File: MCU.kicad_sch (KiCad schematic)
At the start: 0 parts

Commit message: Connected the nucleo to local nets
 - I created all the local lables to the MCU schematic and connected them to the corresponding pins of the Nucleo board.
 - I renumed the hierarchical sheets to be in order of importance
 - I added solder jumpers for making the board more versatile in some cases
 - Corrected the Nucleo pinout on the schematic symbol
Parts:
- added JP? (x6): 0R, symbol Jumper:Jumper_2_Small_Bridged
- added SW?: RESET, Button_Switch_SMD:SW_SPST_SKQG_WithoutStem, symbol Switch:SW_Push
- added U?: NUCLEO64-H503RB, ProjectConnectors:Nucleo64, symbol ProjectMCUs:NUCLEO64-H503RB
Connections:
- new net BTN1: U?.35 (PC2)
- new net BTN2: U?.59 (PC7)
- new net BTN3: U?.1 (PC10)
- new net BTN4: U?.3 (PC12)
- new net BTN5: U?.23 (PC13/BTN2)
- new net BUZZER: JP?.2 (B), JP?.2 (B)
- new net BUZZER_TIM2: U?.28 (PA0)
- new net BUZZER_TIM3: JP?.1 (A), U?.65 (PB4)
- new net E5V: U?.6 (E5V)
- new net GND: SW?.2, U?.19 (GND), U?.20 (GND), U?.22 (GND), U?.47 (GND), U?.58 (GND), U?.8 (GND)
- new net GNDA: U?.70 (AGND)
- new net I2C1_SCL: JP?.1 (A), JP?.2 (B), U?.71 (PC8)
- new net I2C1_SDA: JP?.1 (A), U?.63 (PB10)
- new net I2C_SDA: JP?.2 (B)
- new net I_SENSE: U?.30 (PA1)
- new net JOYSTICK_BTN: U?.66 (PB14)
- new net JOYSTICK_X: U?.37 (PC3)
- new net JOYSTICK_Y: U?.34 (PB0)
- new net LED2: U?.49 (LD2/PA5)
- new net NUCLEO_3V3: U?.16 (+3V3)
- new net NUCLEO_5V: U?.18 (+5V)
- new net NUCLEO_VDD: U?.5 (VDD)
- new net RESETn: SW?.1, U?.14 (~{RESET})
- new net WS2812: JP?.2 (B), JP?.2 (B)
- new net WS2812_PWM: JP?.1 (A), U?.42 (PA10)
- new net WS2812_SPI: JP?.1 (A), U?.53 (PA7)
- new net WS2812_TIM2: JP?.1 (A)
- no-connect marks 0 -> 34

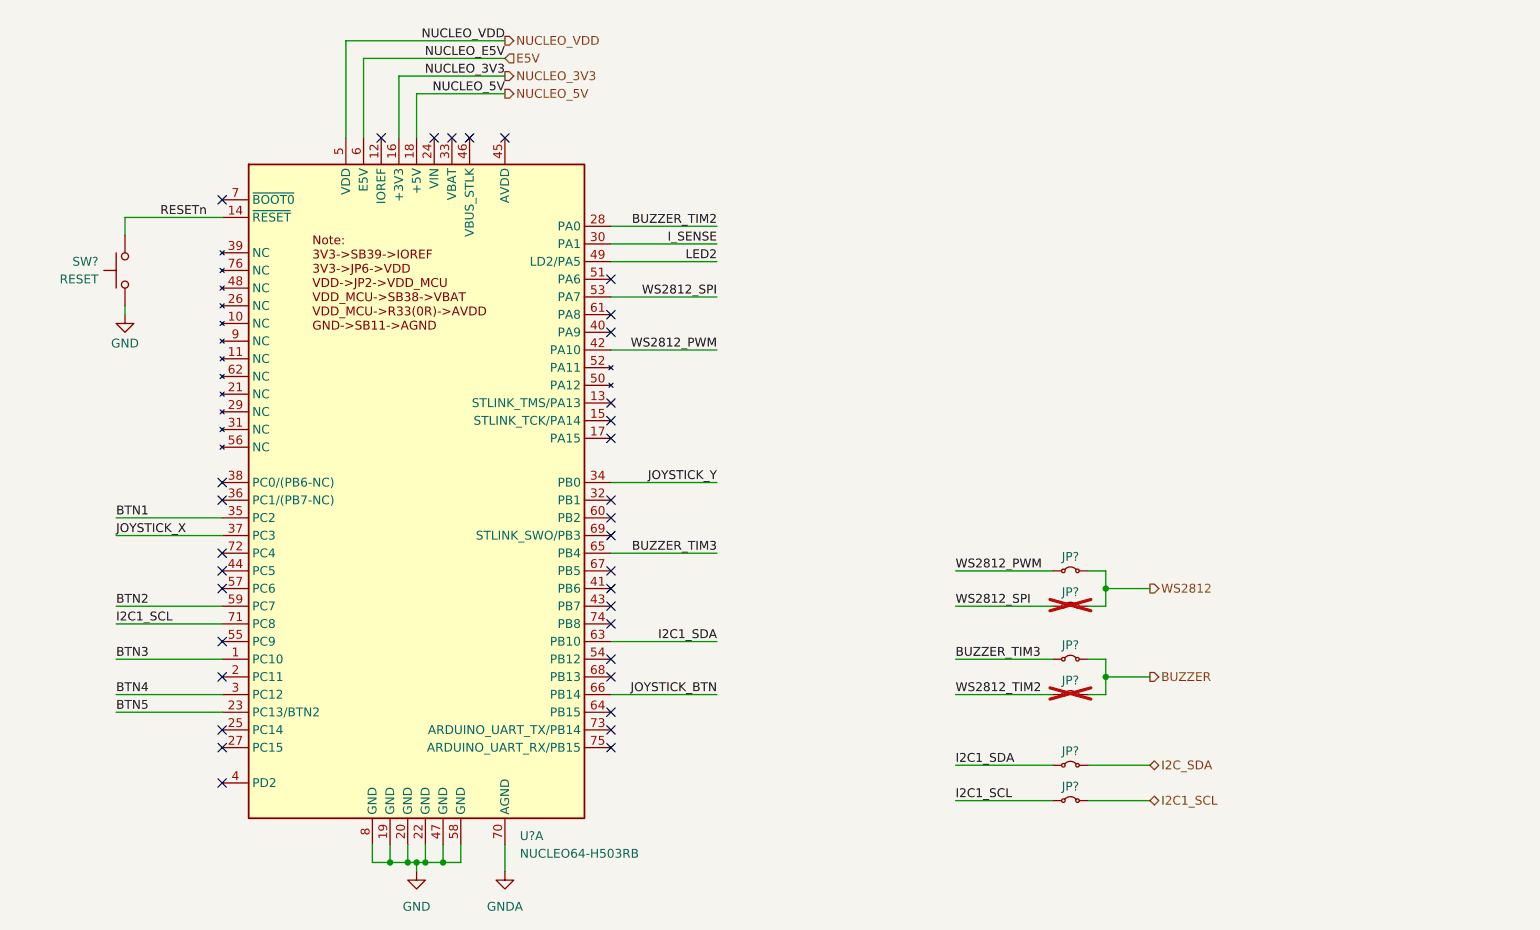
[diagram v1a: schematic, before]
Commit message: Added BME280 on Sensor sheet + Added Power frontend on the dedicated sheet + added I2C Resistors + minor changes
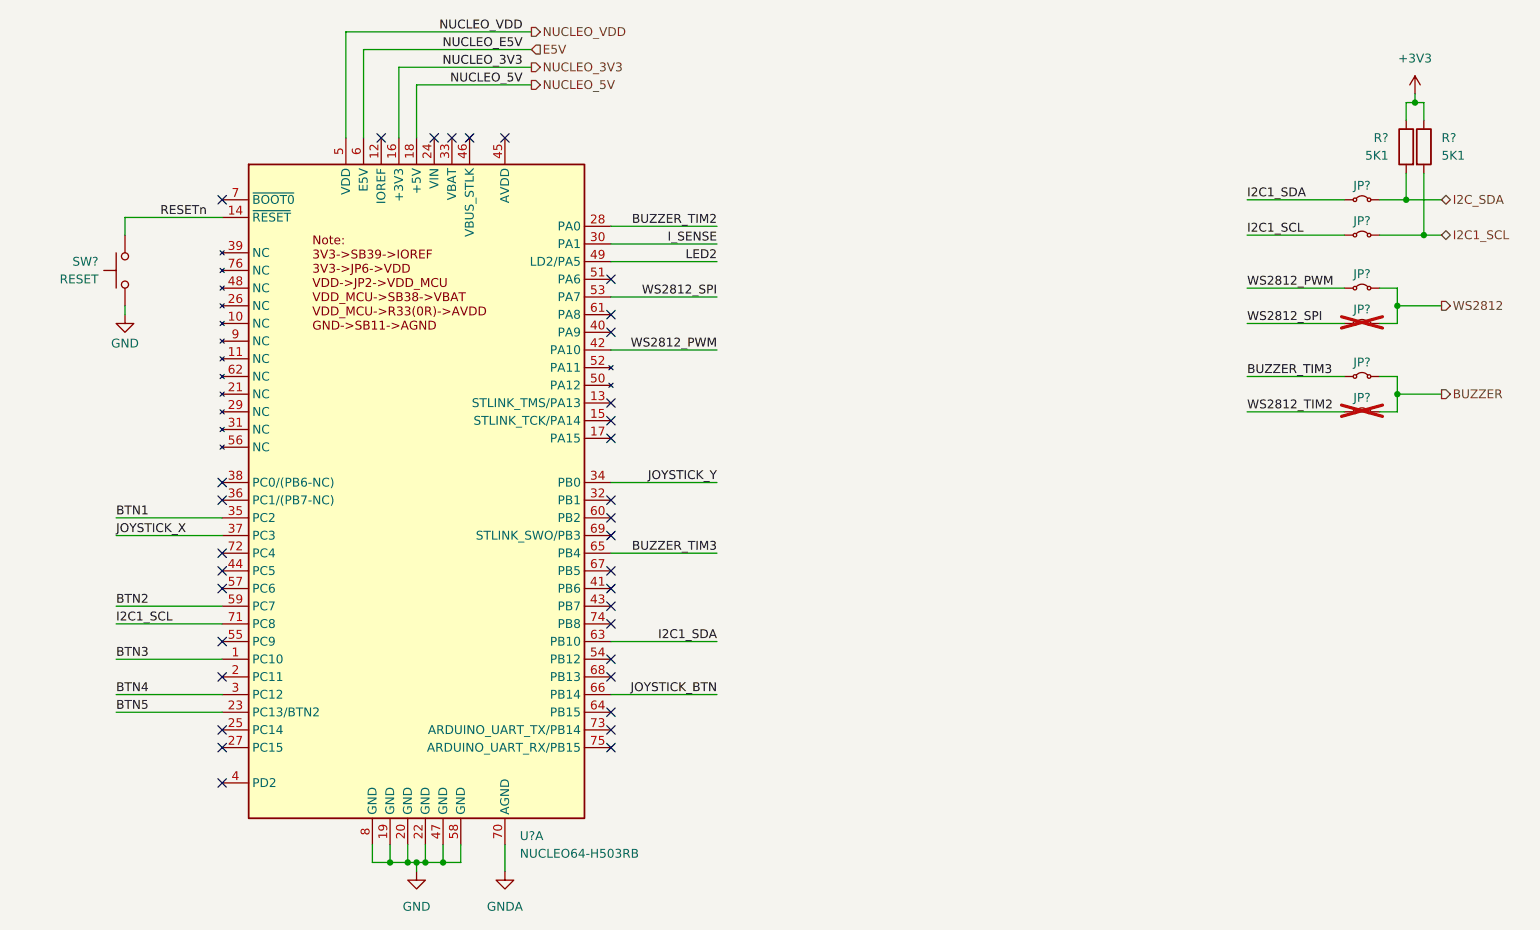
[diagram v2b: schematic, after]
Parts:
- added R? (x2): 5K1, Resistor_SMD:R_0805_2012Metric_Pad1.20x1.40mm_HandSolder, symbol Device:R
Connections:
- net I2C1_SCL: now also R?.2
- net I2C_SDA: now also R?.2
- new net +3V3: R?.1, R?.1
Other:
- moved on the sheet: JP?

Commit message: Small changes
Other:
- moved on the sheet: JP?, R?

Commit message: Added Power connector of the nucleo to the schematic
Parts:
- U?: now left out of the parts list
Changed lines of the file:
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@@
 		(unit 1)
 		(exclude_from_sim no)
-		(in_bom yes)
+		(in_bom no)
 		(on_board yes)
 		(dnp no)
@@
 		(pin "79"
 		)
+		(pin "83"
+		)
+		(pin "90"
+		)
+		(pin "87"
+		)
+		(pin "81"
+		)
+		(pin "84"
+		)
+		(pin "89"
+		)
+		(pin "86"
+		)
+		(pin "82"
+		)
+		(pin "85"
+		)
+		(pin "88"
+		)
 		(instances

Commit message: Added the hierarchical pins of the sheets and connected them, Fixes #7
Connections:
- net BTN1 renamed BTN_1
- net BTN2 renamed BTN_2
- net BTN3 renamed BTN_3
- net BTN4 renamed BTN_4
- net BTN5 renamed BTN_5
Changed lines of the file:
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@@
+		)
+	)
+	(hierarchical_label "JOYSTICK_Y"
+		(shape input)
+		(at 135.89 93.98 0)
+		(effects
+			(font
+				(size 1.27 1.27)
+			)
+			(justify left)
+		)
+	)
+	(hierarchical_label "BTN_1"
+		(shape input)
+		(at 49.53 99.06 180)
+		(effects
+			(font
+				(size 1.27 1.27)
+			)
+			(justify right)
+		)
+	)
+	(hierarchical_label "BTN_3"
+		(shape input)
+		(at 49.53 119.38 180)
+		(effects
+			(font
+				(size 1.27 1.27)
+			)
+			(justify right)
 		)
 	)
@@
 		)
 	)
+	(hierarchical_label "JOYSTICK_BTN"
+		(shape input)
+		(at 135.89 124.46 0)
+		(effects
+			(font
+				(size 1.27 1.27)
+			)
+			(justify left)
+		)
+	)
+	(hierarchical_label "I_SENSE"
+		(shape input)
+		(at 135.89 59.69 0)
+		(effects
+			(font
+				(size 1.27 1.27)
+			)
+			(justify left)
+		)
+	)
+	(hierarchical_label "BTN_4"
+		(shape input)
+		(at 49.53 124.46 180)
+		(effects
+			(font
+				(size 1.27 1.27)
+			)
+			(justify right)
+		)
+	)
+	(hierarchical_label "BTN_5"
+		(shape input)
+		(at 49.53 127 180)
+		(effects
+			(font
+				(size 1.27 1.27)
+			)
+			(justify right)
+		)
+	)
 	(hierarchical_label "BUZZER"
 		(shape output)
@@
 		)
 	)
+	(hierarchical_label "JOYSTICK_X"
+		(shape input)
+		(at 49.53 101.6 180)
+		(effects
+			(font
+				(size 1.27 1.27)
+			)
+			(justify right)
+		)
+	)
+	(hierarchical_label "BTN_2"
+		(shape input)
+		(at 49.53 111.76 180)
+		(effects
+			(font
+				(size 1.27 1.27)
+			)
+			(justify right)
+		)
+	)

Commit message: fixed #1 , added protection circuit 5V selector jumper
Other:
- company: (none) -> Filippo Castellan, Alan Masutti
- title: (none) -> Think Embedded dev Board
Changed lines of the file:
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@@
 	(generator_version "9.0")
 	(paper "A4")
+	(title_block
+		(title "Think Embedded dev Board")
+		(date "2026-03-12")
+		(rev "1.0")
+		(company "Filippo Castellan, Alan Masutti")
+	)
 	(junction
 		(at 93.98 148.59)
@@
 	)
 	(hierarchical_label "NUCLEO_5V"
-		(shape output)
+		(shape input)
 		(at 109.22 36.83 0)
 		(effects

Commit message: Completated the Power Schema + Added Shunts resistors with OP Amp + Connected the RGB Connector to the BUCK (Fixes #5)
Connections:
- net E5V: no longer names the net of U?.6 (E5V)
- net NUCLEO_5V: no longer names the net of U?.18 (+5V)
- no-connect marks 34 -> 36
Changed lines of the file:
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@@
+	)
+	(no_connect
+		(at 92.71 44.45)
 	)
 	(no_connect
@@
 	)
 	(no_connect
+		(at 85.09 44.45)
+	)
+	(no_connect
 		(at 120.65 96.52)
 	)
@@
 	(wire
 		(pts
-			(xy 92.71 36.83) (xy 109.22 36.83)
-		)
-		(stroke
-			(width 0)
-			(type default)
-		)
-	)
-	(wire
-		(pts
 			(xy 92.71 148.59) (xy 92.71 149.86)
 		)
@@
 	(wire
 		(pts
-			(xy 85.09 31.75) (xy 85.09 44.45)
-		)
-		(stroke
-			(width 0)
-			(type default)
-		)
-	)
-	(wire
-		(pts
-			(xy 92.71 36.83) (xy 92.71 44.45)
-		)
-		(stroke
-			(width 0)
-			(type default)
-		)
-	)
-	(wire
-		(pts
 			(xy 49.53 127) (xy 64.77 127)
 		)
@@
 		(pts
 			(xy 90.17 34.29) (xy 90.17 44.45)
-		)
-		(stroke
-			(width 0)
-			(type default)
-		)
-	)
-	(wire
-		(pts
-			(xy 85.09 31.75) (xy 109.22 31.75)
 		)
 		(stroke
@@
 		)
 	)
-	(label "NUCLEO_5V"
-		(at 107.95 36.83 180)
-		(effects
-			(font
-				(size 1.27 1.27)
-			)
-			(justify right bottom)
-		)
-	)
 	(label "NUCLEO_3V3"
 		(at 107.95 34.29 180)
@@
 			)
 			(justify left bottom)
-		)
-	)
-	(label "NUCLEO_E5V"
-		(at 107.95 31.75 180)
-		(effects
-			(font
-				(size 1.27 1.27)
-			)
-			(justify right bottom)
 		)
 	)
@@
 		(shape output)
 		(at 234.95 63.5 0)
-		(effects
-			(font
-				(size 1.27 1.27)
-			)
-			(justify left)
-		)
-	)
-	(hierarchical_label "NUCLEO_5V"
-		(shape input)
-		(at 109.22 36.83 0)
-		(effects
-			(font
-				(size 1.27 1.27)
-			)
-			(justify left)
-		)
-	)
-	(hierarchical_label "E5V"
-		(shape input)
-		(at 109.22 31.75 0)
 		(effects
 			(font
@@
 		(dnp no)
 		(fields_autoplaced yes)
-		(property "Reference" "#PWR?"
+		(property "Reference" "#PWR0114"
 			(at 231.14 36.83 0)
 			(effects
@@
 			(project ""
 				(path "/835b4df9-7d62-45f4-81d2-5a64fbc86f3c/a718e7a0-c449-4532-ac19-5f778084acdd"
-					(reference "#PWR?")
+					(reference "#PWR0114")
 					(unit 1)
 				)
@@
 		(dnp no)
 		(fields_autoplaced yes)
-		(property "Reference" "#PWR?"
+		(property "Reference" "#PWR0113"
 			(at 105.41 156.21 0)
 			(effects
@@
 			(project ""
 				(path "/835b4df9-7d62-45f4-81d2-5a64fbc86f3c/a718e7a0-c449-4532-ac19-5f778084acdd"
-					(reference "#PWR?")
+					(reference "#PWR0113")
 					(unit 1)
 				)
@@
 		(dnp no)
 		(fields_autoplaced yes)
-		(property "Reference" "#PWR?"
+		(property "Reference" "#PWR0111"
 			(at 50.8 76.2 0)
 			(effects
@@
 			(project "Educational-Board_MainBoard"
 				(path "/835b4df9-7d62-45f4-81d2-5a64fbc86f3c/a718e7a0-c449-4532-ac19-5f778084acdd"
-					(reference "#PWR?")
+					(reference "#PWR0111")
 					(unit 1)
 				)
@@
 		(dnp no)
 		(fields_autoplaced yes)
-		(property "Reference" "#PWR?"
+		(property "Reference" "#PWR0112"
 			(at 92.71 156.21 0)
 			(effects
@@
 			(project ""
 				(path "/835b4df9-7d62-45f4-81d2-5a64fbc86f3c/a718e7a0-c449-4532-ac19-5f778084acdd"
-					(reference "#PWR?")
+					(reference "#PWR0112")
 					(unit 1)
 				)
